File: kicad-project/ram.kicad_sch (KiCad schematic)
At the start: 0 parts

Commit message: various things (forgot to commit)
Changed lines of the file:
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@@
 (kicad_sch (version 20211123) (generator eeschema)
   (paper "A4")
+  (hierarchical_label "MSW" (shape input) (at 76.2 76.2 180)
+    (effects (font (size 1.27 1.27)) (justify right))
+  )
   (hierarchical_label "Bus" (shape bidirectional) (at 254 101.6 0)
     (effects (font (size 1.27 1.27)) (justify left))
   )
+  (hierarchical_label "LSW" (shape input) (at 76.2 63.5 180)
+    (effects (font (size 1.27 1.27)) (justify right))
+  )
+  (hierarchical_label "WE" (shape input) (at 76.2 101.6 180)
+    (effects (font (size 1.27 1.27)) (justify right))
+  )
+  (hierarchical_label "RE" (shape input) (at 76.2 88.9 180)
+    (effects (font (size 1.27 1.27)) (justify right))
+  )
 )

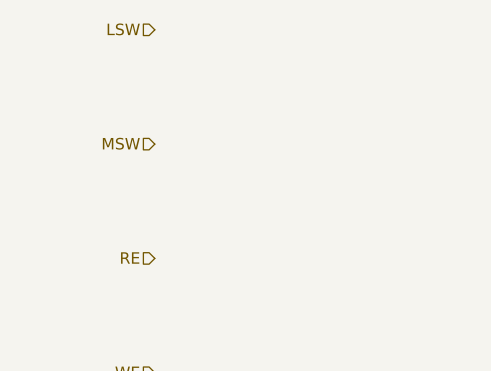
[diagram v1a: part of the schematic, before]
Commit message: update schematic
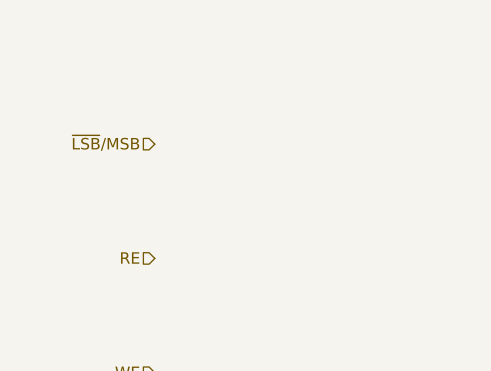
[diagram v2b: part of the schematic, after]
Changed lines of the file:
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@@
 (kicad_sch (version 20211123) (generator eeschema)
   (paper "A4")
-  (hierarchical_label "MSW" (shape input) (at 76.2 76.2 180)
-    (effects (font (size 1.27 1.27)) (justify right))
-  )
   (hierarchical_label "Bus" (shape bidirectional) (at 254 101.6 0)
     (effects (font (size 1.27 1.27)) (justify left))
-  )
-  (hierarchical_label "LSW" (shape input) (at 76.2 63.5 180)
-    (effects (font (size 1.27 1.27)) (justify right))
   )
   (hierarchical_label "WE" (shape input) (at 76.2 101.6 180)
@@
     (effects (font (size 1.27 1.27)) (justify right))
   )
+  (hierarchical_label "~{LSB}{slash}MSB" (shape input) (at 76.2 76.2 180)
+    (effects (font (size 1.27 1.27)) (justify right))
+  )
